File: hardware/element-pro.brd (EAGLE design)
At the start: 50.8 x 50.9 mm, 80 parts, among them J4 AMP FCI 10103594-0001LF, Q3 BSS138PW,115, Q4 BSS138PW,115, SW1 SPST_TACT-KMR2, U1 NEOPIXEL_NANO_2427, U10 TSL2591, U11 915MHz, U12 W25X40CLSNIG-ND-AT25F512BJEDE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, U14 SENSEAIR_S8, U15 VLP-450-F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

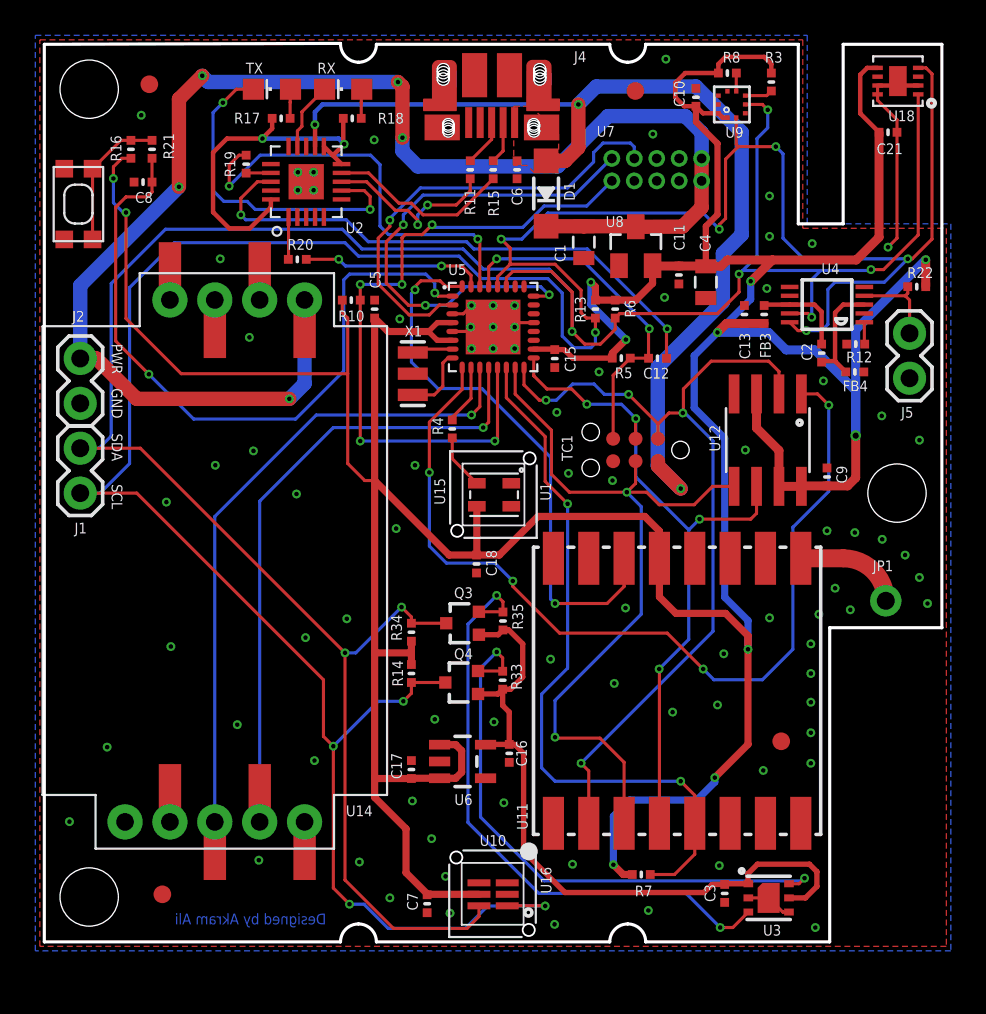
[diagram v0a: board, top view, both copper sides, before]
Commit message: v0.2 - design update
- moved T/RH sensor away from top
- moved thermistor + ADC away from top
- moved VOC sensor from bottom
- repositioned pressure sensor
- added more isolation to all necessary sensors
- a lot of trace and component placement adjustments
- added external voltage input
- ERC/DRC
- silkscreen update
- added gerbers
- NOTE: BOM not updated; untested design
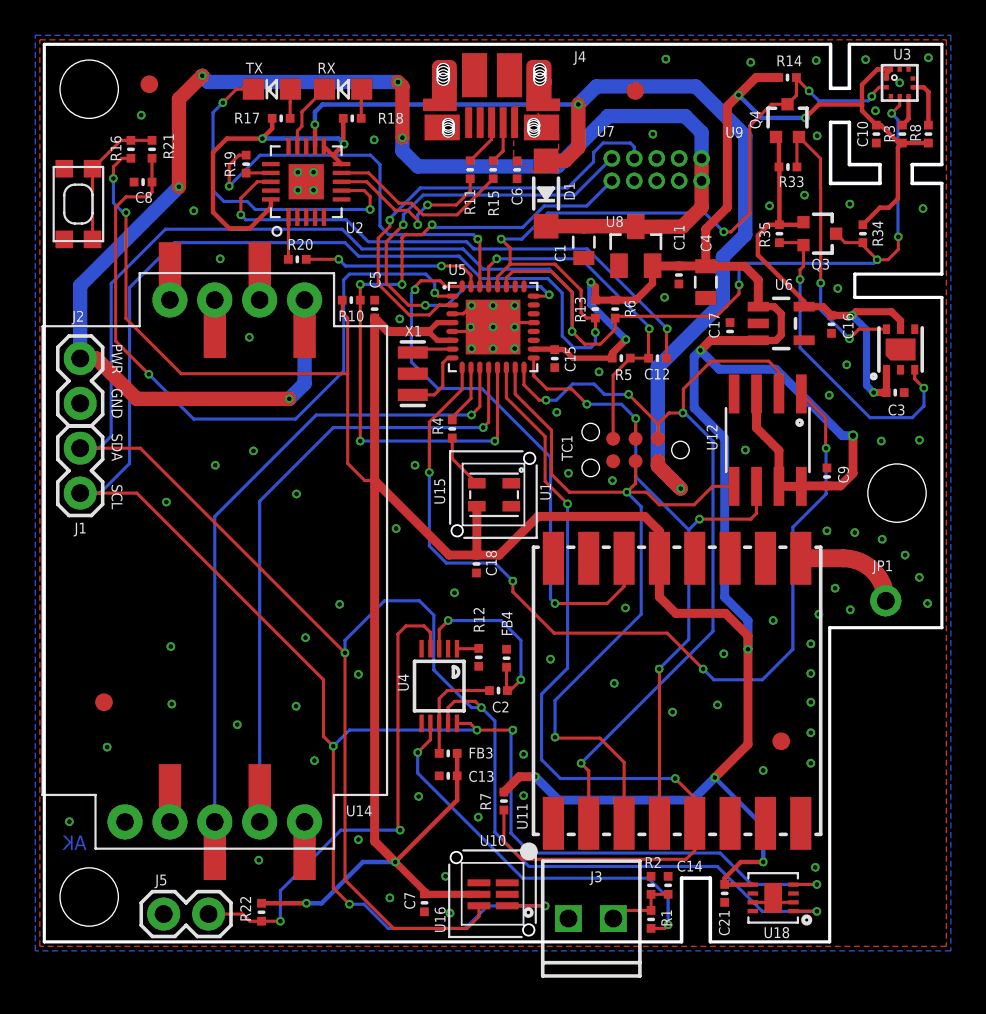
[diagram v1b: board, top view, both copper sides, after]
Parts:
- added C14: 0.1uF, Adafruit Feather 32u4 Bluefruit LE:MICROBUILDER__0402MP
- added J3: (no value), SparkFun-Connectors:1X02_2.54_SCREWTERM
- added R1, R2: 10K, Adafruit Feather 32u4 Bluefruit LE:MICROBUILDER__0402MP
- J1, J2, J5: device SparkFun-Connectors:1X02 -> SparkFun-Connectors:1X02@1
- moved J5 51.5 mm to (9.30, 1.57), turned to 180 degrees
- moved R22 51.3 mm to (12.3, 1.68), turned to 270 degrees
- moved U18 46.8 mm to (41.2, 2.49)
- moved C21 44.1 mm to (38.5, 2.74), turned to 90 degrees
- moved R14 39.9 mm to (42.1, 48.9), turned to 180 degrees
- moved Q4 36.8 mm to (42.1, 46.5), turned to 0 degrees
- moved R34 34.1 mm to (46.3, 40.1), turned to 90 degrees
- moved R33 33.2 mm to (42.1, 43.9), turned to 180 degrees
- moved U3 31.9 mm to (48.5, 33.5), turned to 90 degrees
- moved C13 31.0 mm to (22.9, 9.40), turned to 0 degrees
- moved U4 30.8 mm to (22.4, 14.5), turned to 180 degrees
- moved C17 30.7 mm to (38.8, 34.5)
- moved U6 30.7 mm to (41.7, 35.0)
- moved FB3 30.6 mm to (22.9, 10.7), turned to 0 degrees
- moved C16 30.4 mm to (44.6, 35.0)
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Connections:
- removed net AIN1: U4.5
- new net AIN3: R1.2, U4.7
- new net N$6: C14.2, J3.P2, R1.1, R2.2
- net GND: now also C14.1, J3.P1, R2.1
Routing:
- net SDA: track 145.4 -> 170.8 mm, vias 7 -> 8
- net AIN0: track 5.12 -> 28.4 mm, vias 0 -> 2
- net AIN3: track 0.00 -> 22.8 mm, vias 0 -> 2
- net LSCL: track 33.3 -> 16.7 mm
- net LSDA: track 34.7 -> 18.5 mm
- net 1.8V: track 40.4 -> 26.4 mm, vias 0 -> 2
- net GND: track 19.2 -> 6.77 mm, vias 84 -> 92
- net D10: track 40.3 -> 50.0 mm
- net N$12: track 6.23 -> 11.0 mm, vias 0 -> 2
- net N$6: track 0.00 -> 4.20 mm
- net SCL: track 167.2 -> 170.6 mm, vias 10 -> 11
- net CS: track 1.03 -> 2.86 mm
- net N$15: track 5.27 -> 6.18 mm
- net VCC: track 267.7 -> 267.0 mm, vias 11 -> 14
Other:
- board size 50.8 x 50.9 mm -> 50.8 x 50.8 mm
- board text added: "AK"
- board text added: "v0.2 | May 2019"
- board text removed: "Designed by Akram Ali"
- board text removed: "v0.1 | March 2019"

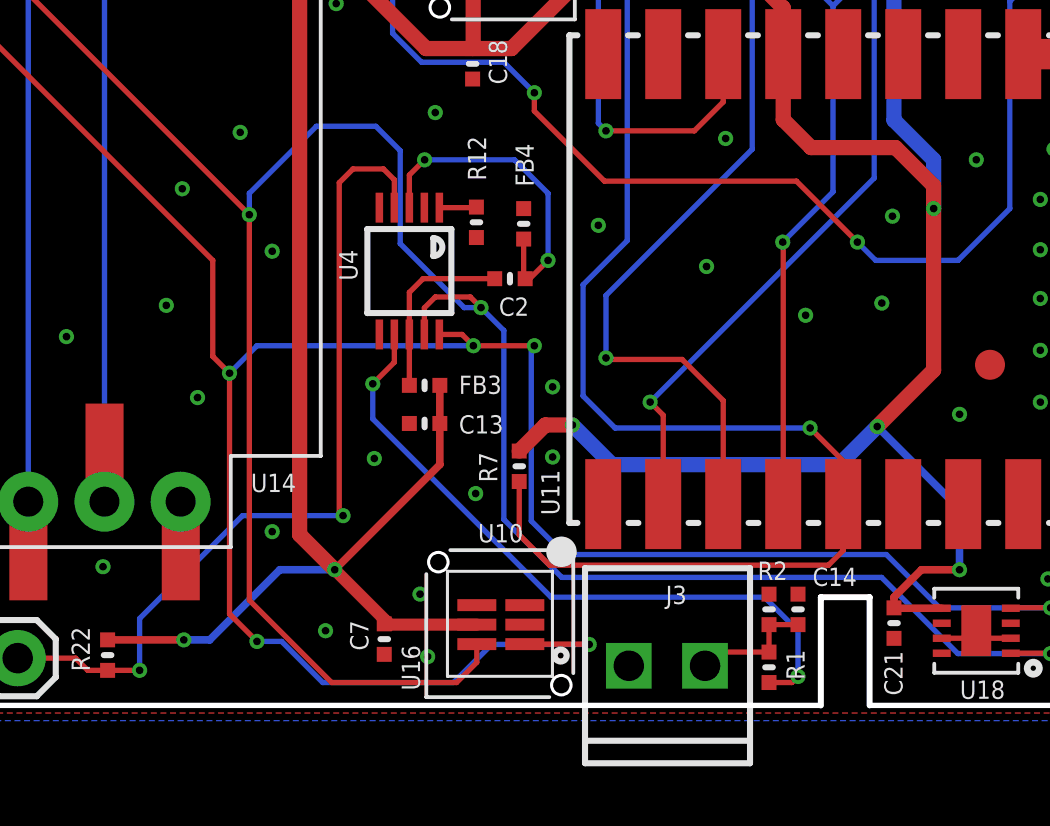
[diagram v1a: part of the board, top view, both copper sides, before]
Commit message: v0.3 update
moved stuff around a bit - functionalluy the same as before.
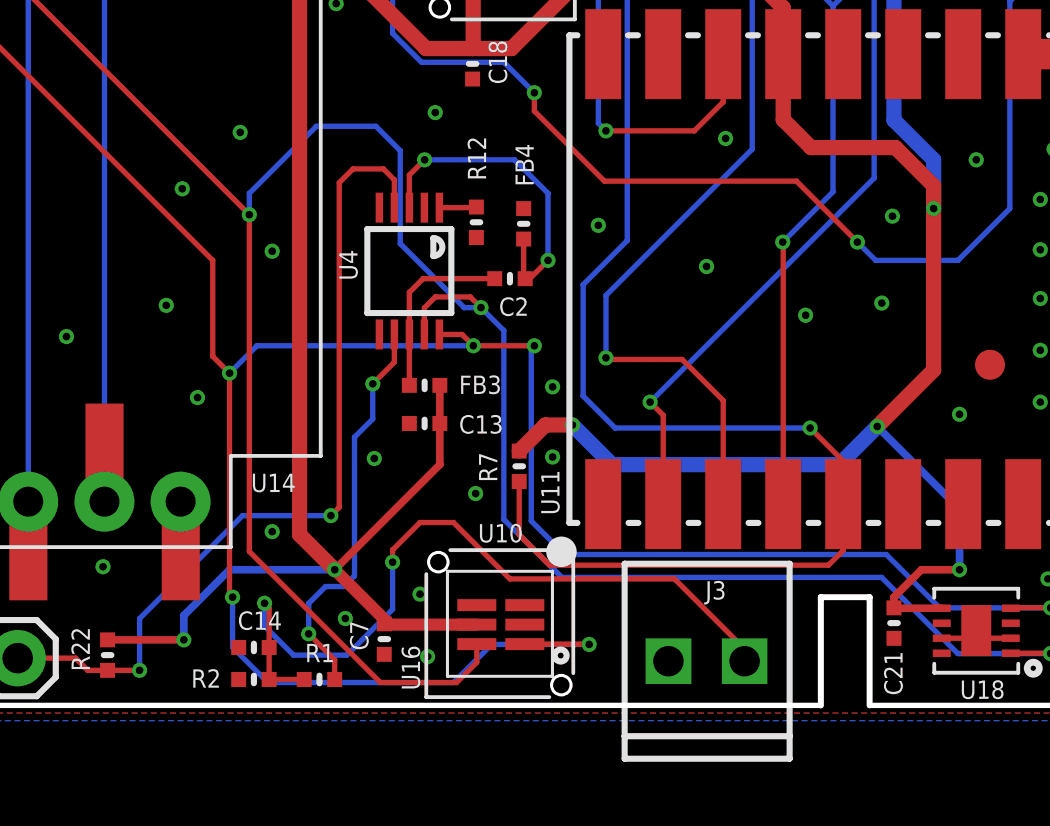
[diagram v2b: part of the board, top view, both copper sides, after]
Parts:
- moved C14 18.2 mm to (17.2, 1.93), turned to 0 degrees
- moved R2 17.3 mm to (17.2, 0.86), turned to 0 degrees
- moved R1 15.0 mm to (19.4, 0.86), turned to 0 degrees
- moved J3 1.33 mm to (33.5, 1.47)
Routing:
- net N$6: track 4.20 -> 26.1 mm, vias 0 -> 2
- net AIN3: track 22.8 -> 13.4 mm
- net SDA: track 170.8 -> 169.8 mm
- net SCL: track 170.6 -> 171.1 mm
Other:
- board text added: "v0.3 | June 2019"
- board text removed: "v0.2 | May 2019"

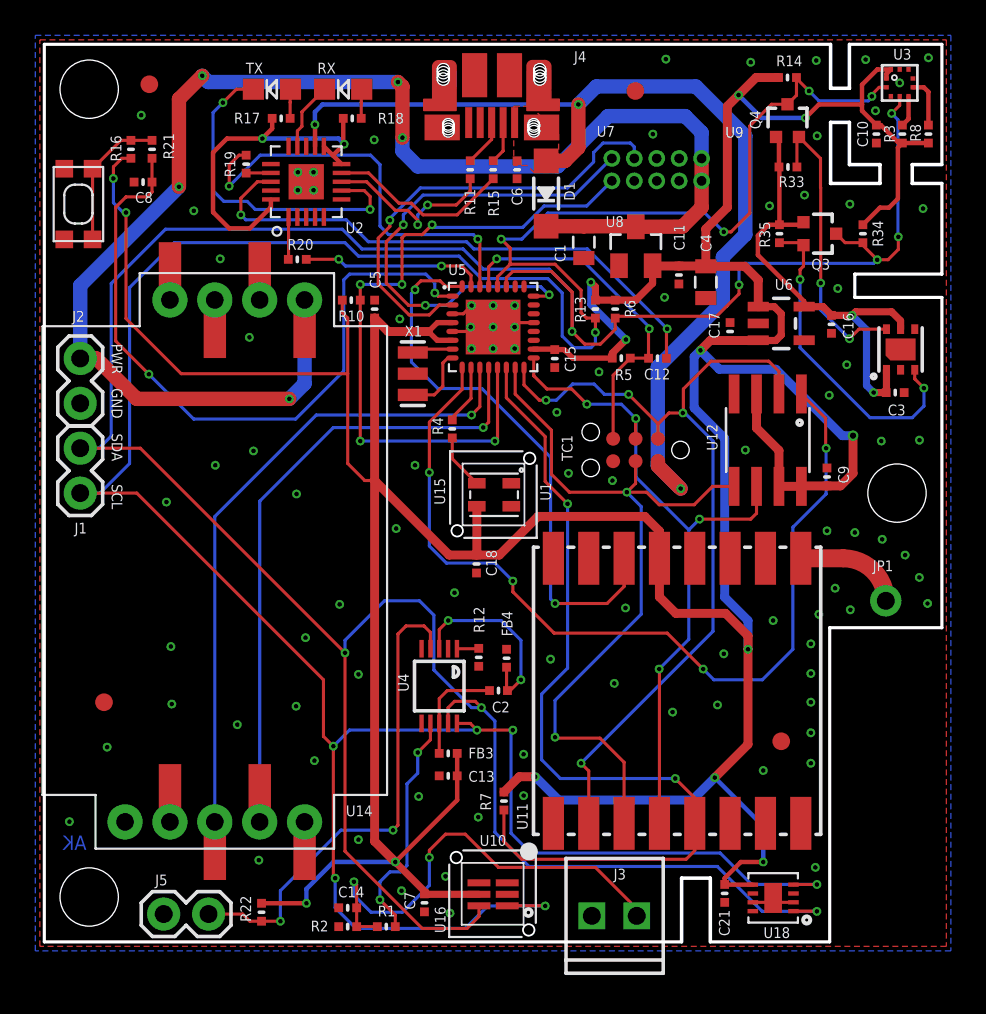
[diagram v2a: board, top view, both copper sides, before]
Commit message: v0.4 - repositioning sensors
- better heat management
- added more thermal breaks on board
- rearranged many traces
- erc/drc
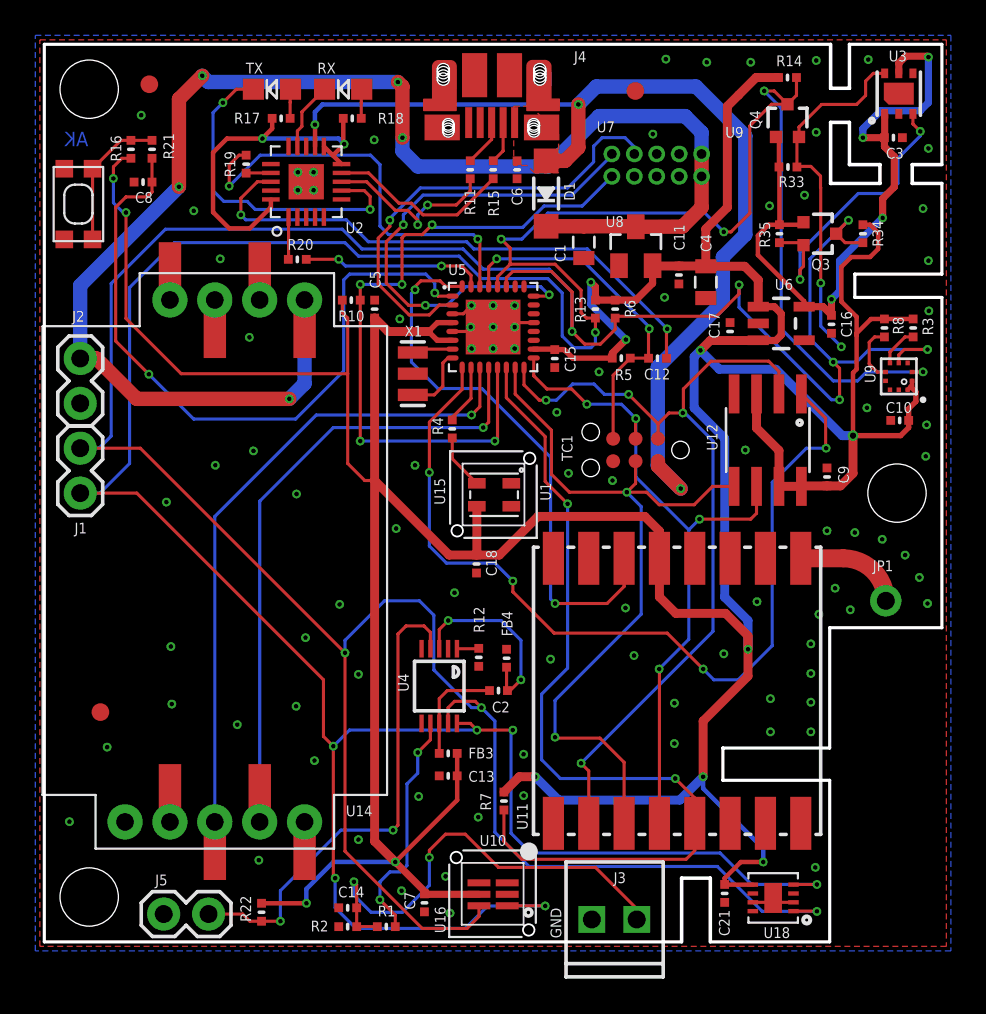
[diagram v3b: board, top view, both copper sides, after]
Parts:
- removed U$7: FIDUCIAL, adafruit:FIDUCIAL_1MM
- moved U9 16.6 mm to (48.4, 32.0), turned to 270 degrees
- moved C10 16.3 mm to (48.4, 29.5), turned to 0 degrees
- moved U3 14.5 mm to (48.4, 48.0)
- moved C3 14.4 mm to (48.1, 45.5)
- moved R8 11.3 mm to (47.5, 34.7), turned to 90 degrees
- moved R3 11.0 mm to (49.2, 34.7), turned to 90 degrees
- moved U$2 0.59 mm to (3.17, 13.0)
- moved U7 0.25 mm to (42.1, 49.5)
- moved J3 0.20 mm to (33.5, 1.27)
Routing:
- net SCL: track 171.1 -> 190.6 mm
- net 1.8V: track 26.4 -> 39.0 mm, vias 2 -> 4
- net SDA: track 169.8 -> 179.0 mm, vias 8 -> 9
- net LSCL: track 16.7 -> 20.6 mm
- net VCC: track 267.5 -> 269.7 mm, vias 14 -> 12
- net LSDA: track 18.5 -> 16.8 mm
- net ADR: track 1.77 -> 2.28 mm
- net GND: vias 92 -> 90
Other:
- outline, holes or cut-outs redrawn
- board text added: "v0.4 | July 2019"
- board text removed: "v0.3 | June 2019"
